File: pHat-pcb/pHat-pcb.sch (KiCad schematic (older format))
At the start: 17 parts, among them J1 Conn_02x20_Odd_Even, J2 Conn_01x24_Male, J3 Conn_Active_High, J4 Conn_Bat, J5 Conn_I2C, J8 Conn_Active_Low, SW1 SW_Push, U1 TPS61023_Breakout, U2 74HC74, U3 DS3231M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

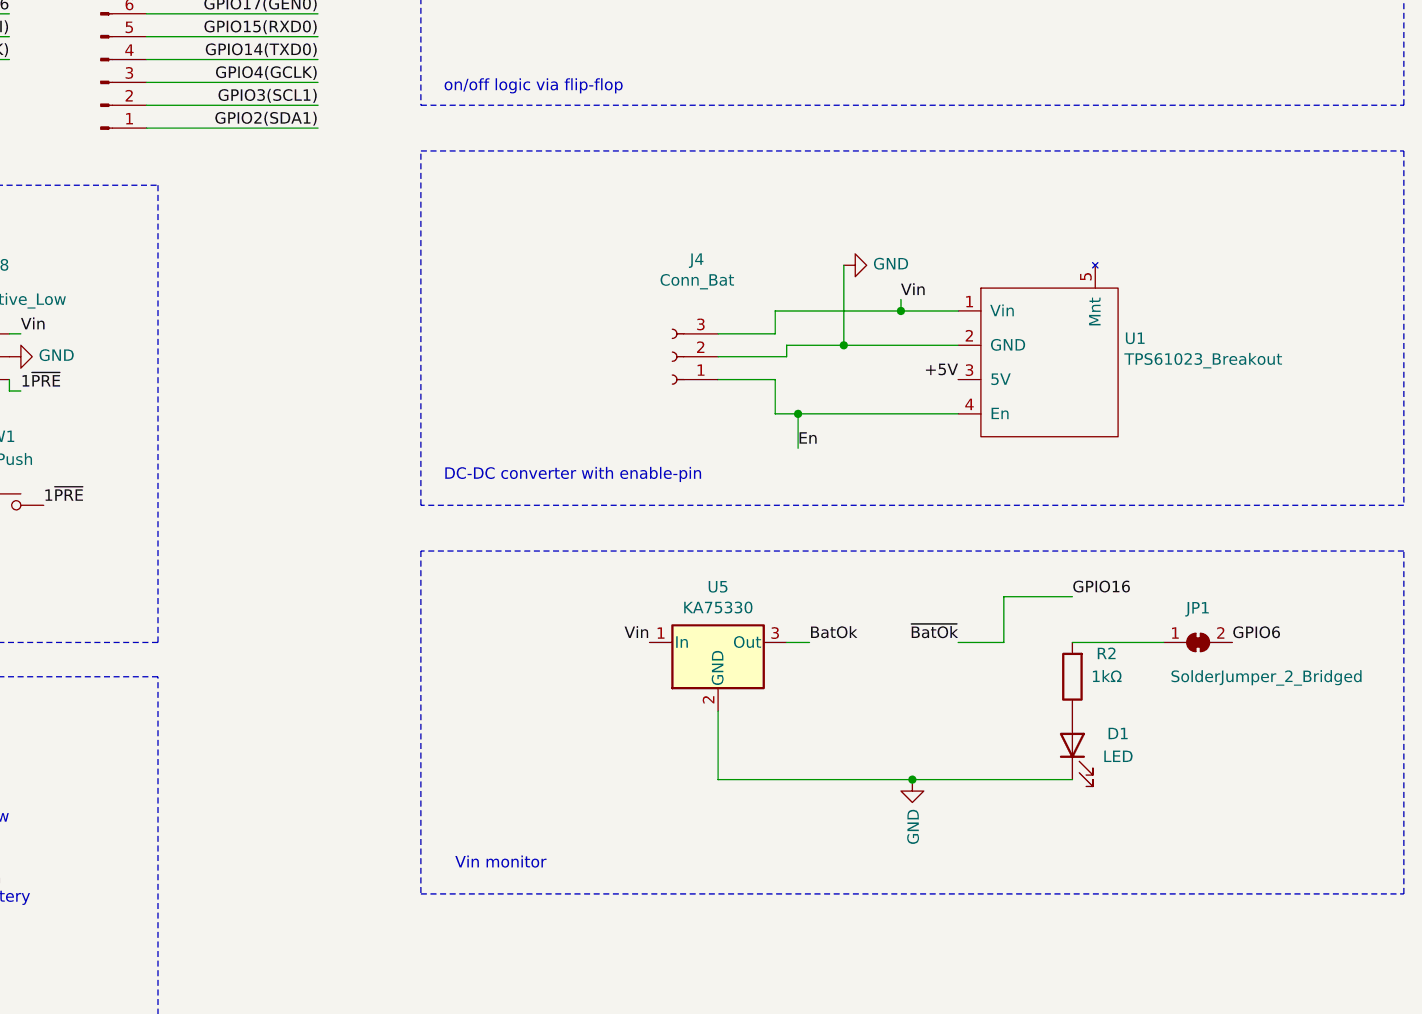
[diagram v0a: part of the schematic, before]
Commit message: Rev6: add connector for 5V, 3V3 and GND
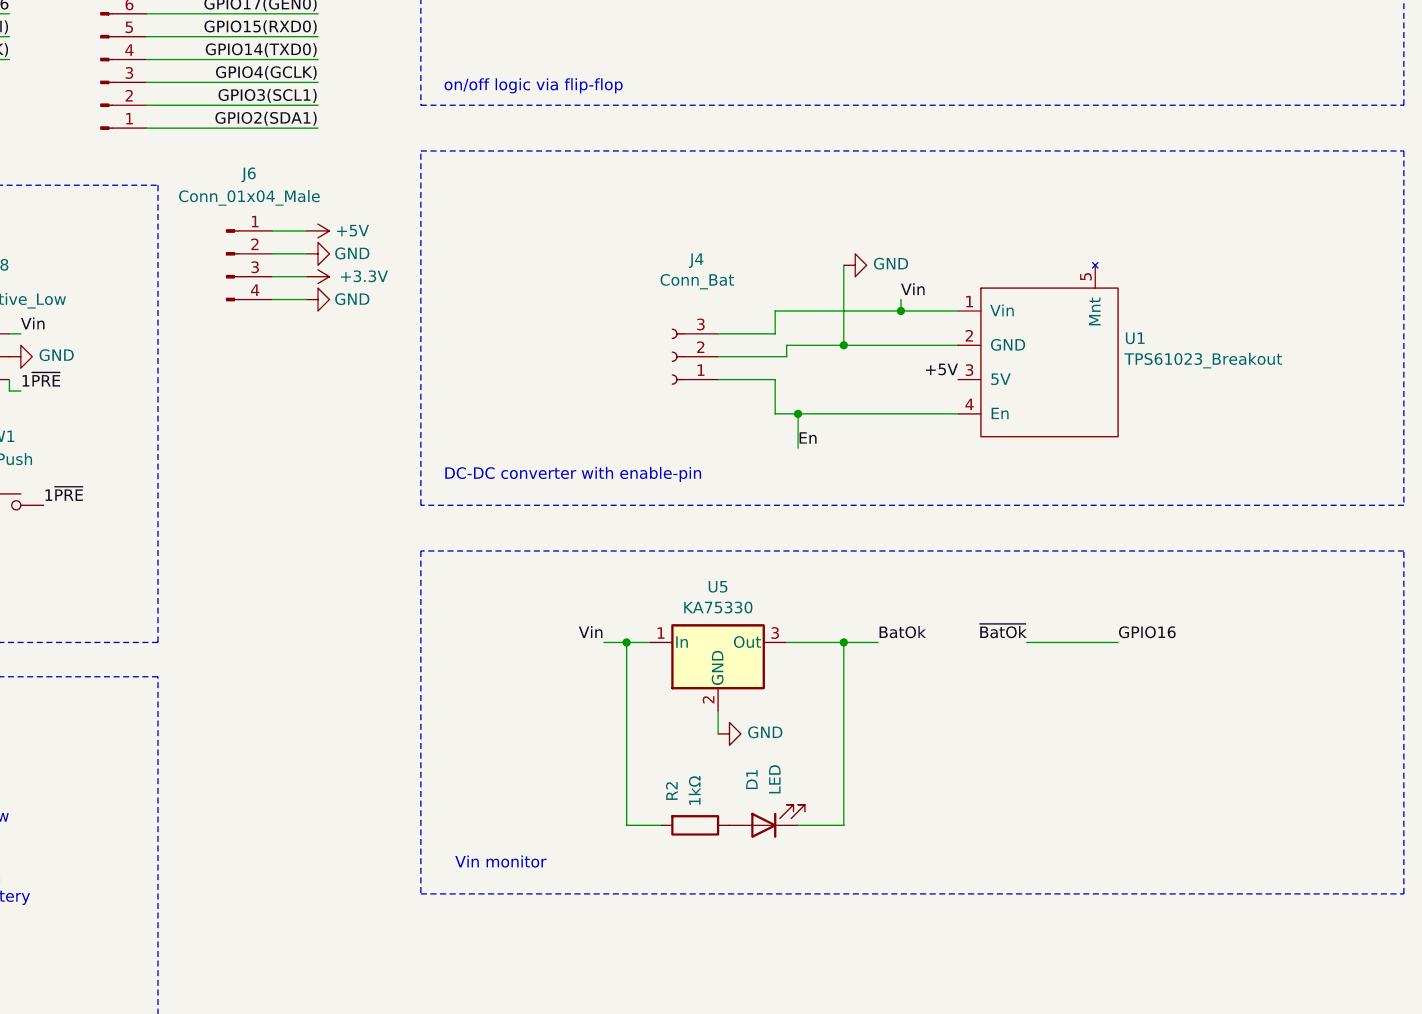
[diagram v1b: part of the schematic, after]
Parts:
- removed JP1: SolderJumper_2_Bridged, Jumper:SolderJumper-2_P1.3mm_Bridged_Pad1.0x1.5mm, symbol Jumper:SolderJumper_2_Bridged
- added J6: Conn_01x04_Male, Connector_PinHeader_2.54mm:PinHeader_1x04_P2.54mm_Vertical, symbol Connector:Conn_01x04_Male
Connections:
- net +3V3: now also J6.3 (Pin_3)
- net +5V: now also J6.1 (Pin_1)
- net BatOk: now also D1.1 (K)
- net GND: now also J6.2 (Pin_2), J6.4 (Pin_4); no longer D1.1 (K)
- net Vin: now also R2.2
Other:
- moved on the sheet: D1, R2
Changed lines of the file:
@@
 Sheet 1 1
 Title "Pi Battery Management pHat"
-Date "2020-10-23"
-Rev "5"
+Date "2020-10-24"
+Rev "6"
 Comp "Bernhard Bablok"
 Comment1 "https://github.com/bablokb/pcb-pi-batman"
@@
 	1    0    0    -1
 $EndComp
-Text Label 6150 5400 2    50   ~ 0
+Text Label 5950 5400 2    50   ~ 0
 Vin
-$Comp
-L power:GND #PWR04
-U 1 1 5F8C6F0E
-P 7300 6000
-F 0 "#PWR04" H 7300 5750 50  0001 C CNN
-F 1 "GND" V 7305 5872 50  0000 R CNN
-F 2 "" H 7300 6000 50  0001 C CNN
-F 3 "" H 7300 6000 50  0001 C CNN
-	1    7300 6000
-	1    0    0    -1
-$EndComp
 $Comp
 L Device:R R2
 U 1 1 5F8C7AC2
-P 8000 5550
-F 0 "R2" H 7850 5450 50  0000 C CNN
-F 1 "1kΩ" H 7850 5550 50  0000 C CNN
-F 2 "Resistor_SMD:R_1206_3216Metric_Pad1.30x1.75mm_HandSolder" V 7930 5550 50  0001 C CNN
-F 3 "~" H 8000 5550 50  0001 C CNN
-	1    8000 5550
-	-1   0    0    1
+P 6350 6200
+F 0 "R2" H 6200 6100 50  0000 C CNN
+F 1 "1kΩ" H 6200 6200 50  0000 C CNN
+F 2 "Resistor_SMD:R_1206_3216Metric_Pad1.30x1.75mm_HandSolder" V 6280 6200 50  0001 C CNN
+F 3 "~" H 6350 6200 50  0001 C CNN
+	1    6350 6200
+	0    1    1    0
 $EndComp
 $Comp
 L Device:LED D1
 U 1 1 5F8C8ABC
-P 8000 5850
-F 0 "D1" V 8050 5650 50  0000 C CNN
-F 1 "LED" V 7950 5650 50  0000 C CNN
-F 2 "LED_SMD:LED_1206_3216Metric_Pad1.42x1.75mm_HandSolder" H 8000 5850 50  0001 C CNN
-F 3 "~" H 8000 5850 50  0001 C CNN
-	1    8000 5850
-	0    -1   -1   0
-$EndComp
-Wire Wire Line
-	6450 5700 6450 6000
-Text Label 6850 5400 0    50   ~ 0
-BatOk
-Wire Wire Line
-	6850 5400 6750 5400
+P 6650 6200
+F 0 "D1" V 6700 6000 50  0000 C CNN
+F 1 "LED" V 6600 6000 50  0000 C CNN
+F 2 "LED_SMD:LED_1206_3216Metric_Pad1.42x1.75mm_HandSolder" H 6650 6200 50  0001 C CNN
+F 3 "~" H 6650 6200 50  0001 C CNN
+	1    6650 6200
+	-1   0    0    1
+$EndComp
 Wire Wire Line
 	1450 6500 1950 6500
@@
 Wire Wire Line
 	2550 6500 2750 6500
-Text Label 7500 5400 2    50   ~ 0
+Text Label 7800 5400 2    50   ~ 0
 ~BatOk
-Text Label 8000 5200 0    50   ~ 0
+Text Label 8200 5400 0    50   ~ 0
 GPIO16
-Connection ~ 7300 6000
-Wire Wire Line
-	7300 6000 8000 6000
-Wire Wire Line
-	6450 6000 7300 6000
 Wire Notes Line
 	9450 5000 5150 5000
@@
 Wire Wire Line
 	1850 6600 1850 6700
-$Comp
-L Jumper:SolderJumper_2_Bridged JP1
-U 1 1 5F9ABDE0
-P 8550 5400
-F 0 "JP1" H 8550 5550 50  0000 C CNN
-F 1 "SolderJumper_2_Bridged" H 8850 5250 50  0000 C CNN
-F 2 "Jumper:SolderJumper-2_P1.3mm_Bridged_Pad1.0x1.5mm" H 8550 5400 50  0001 C CNN
-F 3 "~" H 8550 5400 50  0001 C CNN
-	1    8550 5400
-	1    0    0    -1
-$EndComp
-Wire Wire Line
-	8000 5400 8400 5400
-Text Label 8700 5400 0    50   ~ 0
-GPIO6
-Wire Wire Line
-	7500 5400 7700 5400
-Wire Wire Line
-	7700 5400 7700 5200
-Wire Wire Line
-	7700 5200 8000 5200
 NoConn ~ 2550 6600
+$Comp
+L Connector:Conn_01x04_Male J6
+U 1 1 5F948FB5
+P 4300 3700
+F 0 "J6" H 4400 4050 50  0000 C CNN
+F 1 "Conn_01x04_Male" H 4400 3950 50  0000 C CNN
+F 2 "Connector_PinHeader_2.54mm:PinHeader_1x04_P2.54mm_Vertical" H 4300 3700 50  0001 C CNN
+F 3 "~" H 4300 3700 50  0001 C CNN
+	1    4300 3700
+	1    0    0    -1
+$EndComp
+$Comp
+L power:+5V #PWR05
+U 1 1 5F949842
+P 4650 3600
+F 0 "#PWR05" H 4650 3450 50  0001 C CNN
+F 1 "+5V" V 4650 3800 50  0000 C CNN
+F 2 "" H 4650 3600 50  0000 C CNN
+F 3 "" H 4650 3600 50  0000 C CNN
+	1    4650 3600
+	0    1    1    0
+$EndComp
+$Comp
+L power:+3.3V #PWR07
+U 1 1 5F94A6C5
+P 4650 3800
+F 0 "#PWR07" H 4650 3650 50  0001 C CNN
+F 1 "+3.3V" V 4650 4050 50  0000 C CNN
+F 2 "" H 4650 3800 50  0000 C CNN
+F 3 "" H 4650 3800 50  0000 C CNN
+	1    4650 3800
+	0    1    1    0
+$EndComp
+$Comp
+L power:GND #PWR06
+U 1 1 5F94AF46
+P 4650 3700
+F 0 "#PWR06" H 4650 3450 50  0001 C CNN
+F 1 "GND" V 4650 3500 50  0000 C CNN
+F 2 "" H 4650 3700 50  0000 C CNN
+F 3 "" H 4650 3700 50  0000 C CNN
+	1    4650 3700
+	0    -1   -1   0
+$EndComp
+$Comp
+L power:GND #PWR08
+U 1 1 5F94B7FD
+P 4650 3900
+F 0 "#PWR08" H 4650 3650 50  0001 C CNN
+F 1 "GND" V 4650 3700 50  0000 C CNN
+F 2 "" H 4650 3900 50  0000 C CNN
+F 3 "" H 4650 3900 50  0000 C CNN
+	1    4650 3900
+	0    -1   -1   0
+$EndComp
+Wire Wire Line
+	4500 3600 4650 3600
+Wire Wire Line
+	4500 3700 4650 3700
+Wire Wire Line
+	4500 3800 4650 3800
+Wire Wire Line
+	4500 3900 4650 3900
+$Comp
+L power:GND #PWR04
+U 1 1 5F8C6F0E
+P 6450 5800
+F 0 "#PWR04" H 6450 5550 50  0001 C CNN
+F 1 "GND" V 6455 5672 50  0000 R CNN
+F 2 "" H 6450 5800 50  0001 C CNN
+F 3 "" H 6450 5800 50  0001 C CNN
+	1    6450 5800
+	0    -1   -1   0
+$EndComp
+Wire Wire Line
+	6450 5700 6450 5800
+Wire Wire Line
+	6150 5400 6050 5400
+Wire Wire Line
+	6050 5400 6050 6200
+Wire Wire Line
+	6050 6200 6200 6200
+Connection ~ 6050 5400
+Wire Wire Line
+	6050 5400 5950 5400
+Wire Wire Line
+	6800 6200 7000 6200
+Wire Wire Line
+	7000 6200 7000 5400
+Wire Wire Line
+	6750 5400 7000 5400
+Connection ~ 7000 5400
+Wire Wire Line
+	7000 5400 7150 5400
+Text Label 7150 5400 0    50   ~ 0
+BatOk
+Wire Wire Line
+	7800 5400 8200 5400
 $EndSCHEMATC

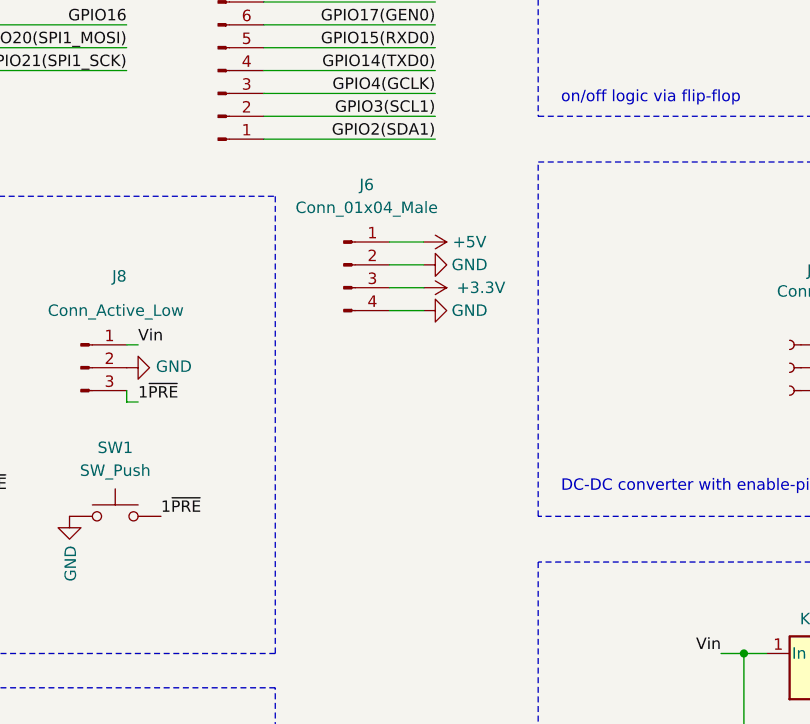
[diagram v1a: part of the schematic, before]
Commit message: Rev7: added shutdown-button
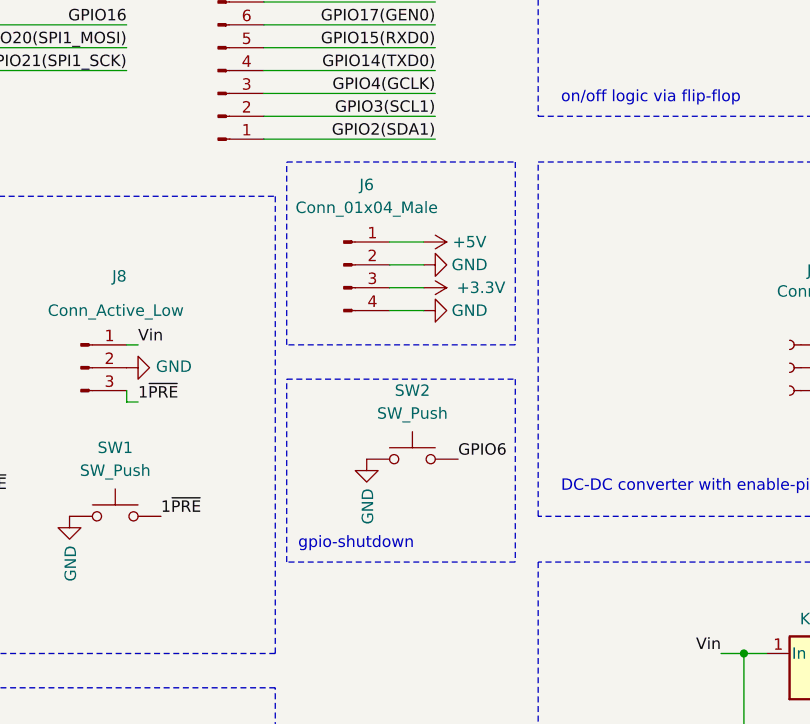
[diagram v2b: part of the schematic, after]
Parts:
- added SW2: SW_Push, user:SW_PUSH_SLIM_1x4, symbol Switch:SW_Push
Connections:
- net GND: now also SW2.1
- net GPIO6: now also SW2.2
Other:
- note added: "gpio-shutdown"
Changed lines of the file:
@@
 Sheet 1 1
 Title "Pi Battery Management pHat"
-Date "2020-10-24"
-Rev "6"
+Date "2020-10-28"
+Rev "7"
 Comp "Bernhard Bablok"
 Comment1 "https://github.com/bablokb/pcb-pi-batman"
@@
 Wire Wire Line
 	7800 5400 8200 5400
+Wire Notes Line
+	4050 3250 5050 3250
+Wire Notes Line
+	5050 3250 5050 4050
+Wire Notes Line
+	5050 4050 4050 4050
+Wire Notes Line
+	4050 4050 4050 3250
+$Comp
+L Switch:SW_Push SW2
+U 1 1 5F9A4237
+P 4600 4550
+F 0 "SW2" H 4600 4850 50  0000 C CNN
+F 1 "SW_Push" H 4600 4750 50  0000 C CNN
+F 2 "user:SW_PUSH_SLIM_1x4" H 4600 4750 50  0001 C CNN
+F 3 "~" H 4600 4750 50  0001 C CNN
+	1    4600 4550
+	1    0    0    -1
+$EndComp
+$Comp
+L power:GND #PWR09
+U 1 1 5F9A4B7E
+P 4400 4550
+F 0 "#PWR09" H 4400 4300 50  0001 C CNN
+F 1 "GND" V 4405 4422 50  0000 R CNN
+F 2 "" H 4400 4550 50  0001 C CNN
+F 3 "" H 4400 4550 50  0001 C CNN
+	1    4400 4550
+	1    0    0    -1
+$EndComp
+Text Label 4800 4550 0    50   ~ 0
+GPIO6
+Wire Notes Line
+	4050 4200 5050 4200
+Wire Notes Line
+	5050 4200 5050 5000
+Wire Notes Line
+	5050 5000 4050 5000
+Wire Notes Line
+	4050 5000 4050 4200
+Text Notes 4100 4950 0    50   ~ 0
+gpio-shutdown
 $EndSCHEMATC

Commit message: Rev8: add 5V to external battery connector / fixed KA75330 pin-order / updated labels
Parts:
- J4: footprint TerminalBlock_TE-Connectivity:TerminalBlock_TE_282834-3_1x03_P2.54mm_Horizontal -> TerminalBlock_TE-Connectivity:TerminalBlock_TE_282834-4_1x04_P2.54mm_Horizontal; symbol Connector:Conn_01x03_Female -> Connector:Conn_01x04_Female
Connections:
- net +5V: now also J4.2 (Pin_2)
- net GND: now also J4.3 (Pin_3); no longer J4.2 (Pin_2)
- net Vin: now also J4.4 (Pin_4); no longer J4.3 (Pin_3)
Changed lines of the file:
@@
 Sheet 1 1
 Title "Pi Battery Management pHat"
-Date "2020-10-28"
-Rev "7"
+Date "2020-10-30"
+Rev "8"
 Comp "Bernhard Bablok"
 Comment1 "https://github.com/bablokb/pcb-pi-batman"
@@
 Wire Wire Line
 	6950 950  7550 950
-Text Label 6800 4550 0    50   ~ 0
+Text Label 7500 4400 2    50   ~ 0
 En
 $Comp
@@
 $EndComp
 $Comp
-L Connector:Conn_01x03_Female J4
+L Connector:Conn_01x04_Female J4
 U 1 1 5F762AD7
 P 6250 4150
 F 0 "J4" H 6142 3725 50  0000 C CNN
 F 1 "Conn_Bat" H 6142 3816 50  0000 C CNN
-F 2 "TerminalBlock_TE-Connectivity:TerminalBlock_TE_282834-3_1x03_P2.54mm_Horizontal" H 6250 4150 50  0001 C CNN
+F 2 "TerminalBlock_TE-Connectivity:TerminalBlock_TE_282834-4_1x04_P2.54mm_Horizontal" H 6250 4150 50  0001 C CNN
 F 3 "~" H 6250 4150 50  0001 C CNN
 	1    6250 4150
 	-1   0    0    1
 $EndComp
-Wire Wire Line
-	6450 4050 6700 4050
-Wire Wire Line
-	6700 4050 6700 3950
-Wire Wire Line
-	6750 4150 6750 4100
-Wire Wire Line
-	6450 4150 6750 4150
 Text Label 7500 4250 2    50   ~ 0
 +5V
@@
 Wire Notes Line
 	650  5400 650  3400
-Wire Wire Line
-	6800 4550 6800 4400
 Text Label 8600 1350 0    50   ~ 0
 En
@@
 Wire Wire Line
 	6700 4250 6700 4400
-Wire Wire Line
-	6700 4400 6800 4400
-Connection ~ 6800 4400
 Wire Wire Line
 	8800 1100 8650 1100
@@
 Text Label 2650 4700 0    50   ~ 0
 1~PRE
-Wire Wire Line
-	6750 4100 7000 4100
-Wire Wire Line
-	6800 4400 7500 4400
 Wire Wire Line
 	7000 3750 7000 4100
@@
 Text Notes 2800 6200 0    50   ~ 0
 on: High -> Low
-Text Label 7250 3900 0    50   ~ 0
+Text Label 7500 3950 2    50   ~ 0
 Vin
-Wire Wire Line
-	7250 3900 7250 3950
-Connection ~ 7250 3950
-Wire Wire Line
-	7250 3950 7500 3950
-Wire Wire Line
-	6700 3950 7250 3950
 Text Label 1400 4000 2    50   ~ 0
 GPIO2(SDA1)
@@
 Wire Wire Line
 	1950 4200 2050 4200
-$Comp
-L User:KA75330 U5
-U 1 1 5F8B41F9
-P 6450 5400
-F 0 "U5" H 6450 5642 50  0000 C CNN
-F 1 "KA75330" H 6450 5551 50  0000 C CNN
-F 2 "Package_TO_SOT_THT:TO-92_Inline_Wide" H 6450 5625 50  0001 C CIN
-F 3 "" H 6450 5350 50  0001 C CNN
-	1    6450 5400
-	1    0    0    -1
-$EndComp
 Text Label 5950 5400 2    50   ~ 0
 Vin
@@
 Text Notes 4100 4950 0    50   ~ 0
 gpio-shutdown
+Wire Wire Line
+	6700 4100 6700 4050
+Wire Wire Line
+	6700 4050 6450 4050
+Wire Wire Line
+	6700 4100 7000 4100
+Wire Wire Line
+	7500 4250 6800 4250
+Wire Wire Line
+	6800 4250 6800 4150
+Wire Wire Line
+	6800 4150 6450 4150
+Wire Wire Line
+	6450 3950 7500 3950
+Wire Wire Line
+	6700 4400 7500 4400
+$Comp
+L User:KA75330 U5
+U 1 1 5F8B41F9
+P 6450 5400
+F 0 "U5" H 6450 5642 50  0000 C CNN
+F 1 "KA75330" H 6450 5551 50  0000 C CNN
+F 2 "Package_TO_SOT_THT:TO-92_Inline_Wide" H 6450 5625 50  0001 C CIN
+F 3 "" H 6450 5350 50  0001 C CNN
+	1    6450 5400
+	1    0    0    -1
+$EndComp
 $EndSCHEMATC

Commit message: bugfix: prevent 2nd flip-flop from floating
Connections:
- net GND: now also U2.11 (2CLK), U2.12 (2D)
- net Vin: now also U2.10 (2~PRE), U2.13 (2~CLR)
- no-connect marks 14 -> 10
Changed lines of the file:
@@
 Sheet 1 1
 Title "Pi Battery Management pHat"
-Date "2020-10-30"
-Rev "8"
+Date "2020-12-15"
+Rev "9"
 Comp "Bernhard Bablok"
 Comment1 "https://github.com/bablokb/pcb-pi-batman"
@@
 NoConn ~ 8600 1550
 NoConn ~ 8600 1650
-NoConn ~ 7900 1550
-NoConn ~ 7900 1650
-NoConn ~ 7900 1750
-NoConn ~ 7900 1850
 Wire Wire Line
 	7550 950  7550 1250
@@
 $EndComp
 Wire Wire Line
-	7550 950  8400 950
+	7550 950  7750 950
 $Comp
 L power:PWR_FLAG #FLG02
@@
 	1    0    0    -1
 $EndComp
+Wire Wire Line
+	7900 1650 7750 1650
+Wire Wire Line
+	7750 1650 7750 950
+Connection ~ 7750 950
+Wire Wire Line
+	7750 950  8400 950
+Wire Wire Line
+	7900 1850 7750 1850
+Wire Wire Line
+	7750 1850 7750 1650
+Connection ~ 7750 1650
+Wire Wire Line
+	7900 1550 7800 1550
+Wire Wire Line
+	7800 1550 7800 1750
+Wire Wire Line
+	7800 2050 8400 2050
+Connection ~ 8400 2050
+Wire Wire Line
+	7900 1750 7800 1750
+Connection ~ 7800 1750
+Wire Wire Line
+	7800 1750 7800 2050
 $EndSCHEMATC
